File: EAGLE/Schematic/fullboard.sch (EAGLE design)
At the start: 101 parts, among them CN1 B4B-ZR, CN2 B4B-ZR, CN3 B4B-ZR, CN4 S4B-ZR, CN5 S4B-ZR, CN6 S4B-ZR, CN7 S4B-ZR, CN8 S4B-ZR, CN9 S4B-ZR, IC1 IFX007T, IC2 IFX007T, IC3 IFX007T, IC4 IFX007T, J1 10118193-0001LF, Q1 8MHz ±10ppm Crystal 18pF 80 O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, SW1 TR1-SPST, U1 ATXMEGA128A3U-AU, U2 FT232RL-REEL

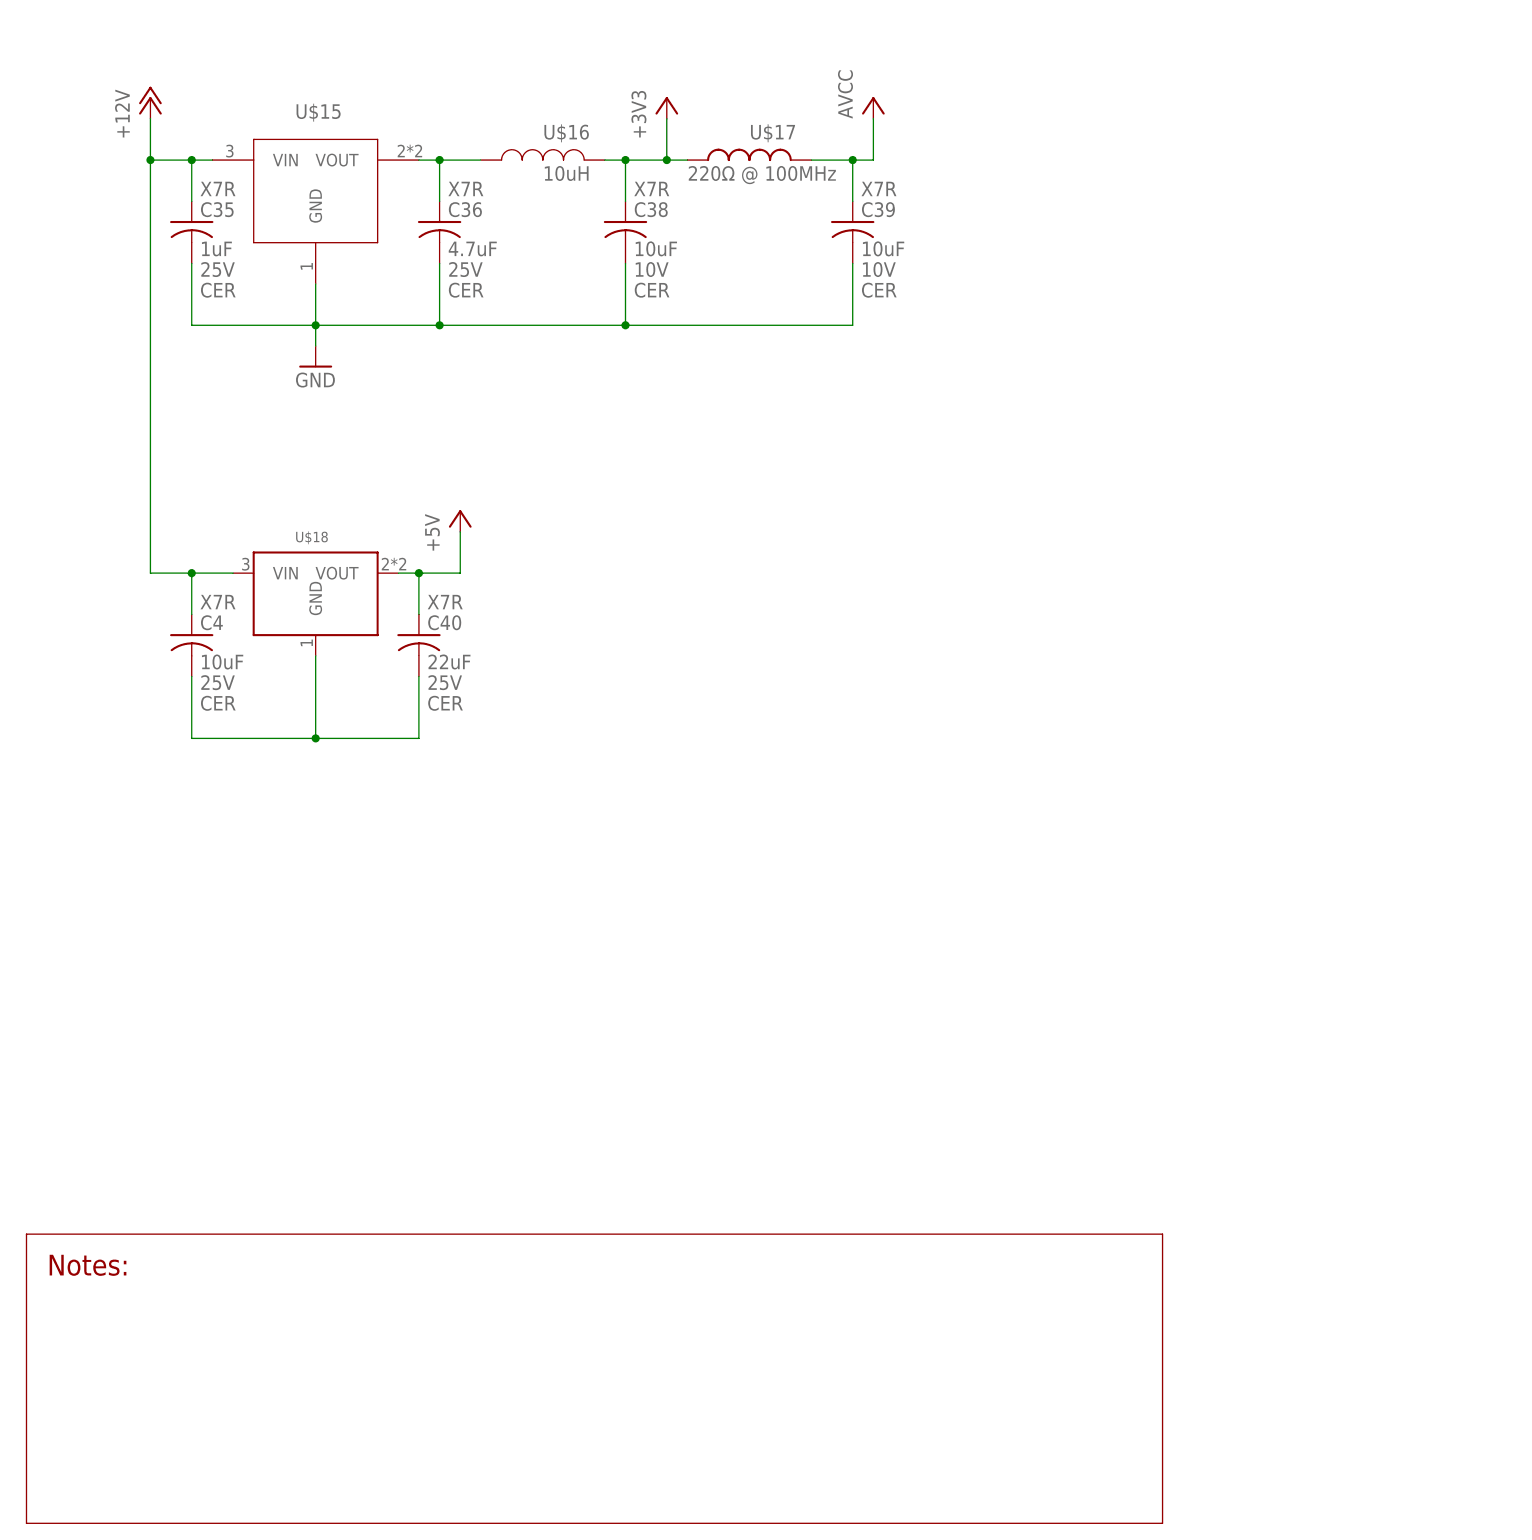
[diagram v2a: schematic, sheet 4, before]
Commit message: V0.3
Don't you dare put a fucking fuse holder on the board.

Added:
* Routing all the remaining signals
* Vias for breakout of leftover pins
* Now with 200% more suffering

Still to do:
* Things
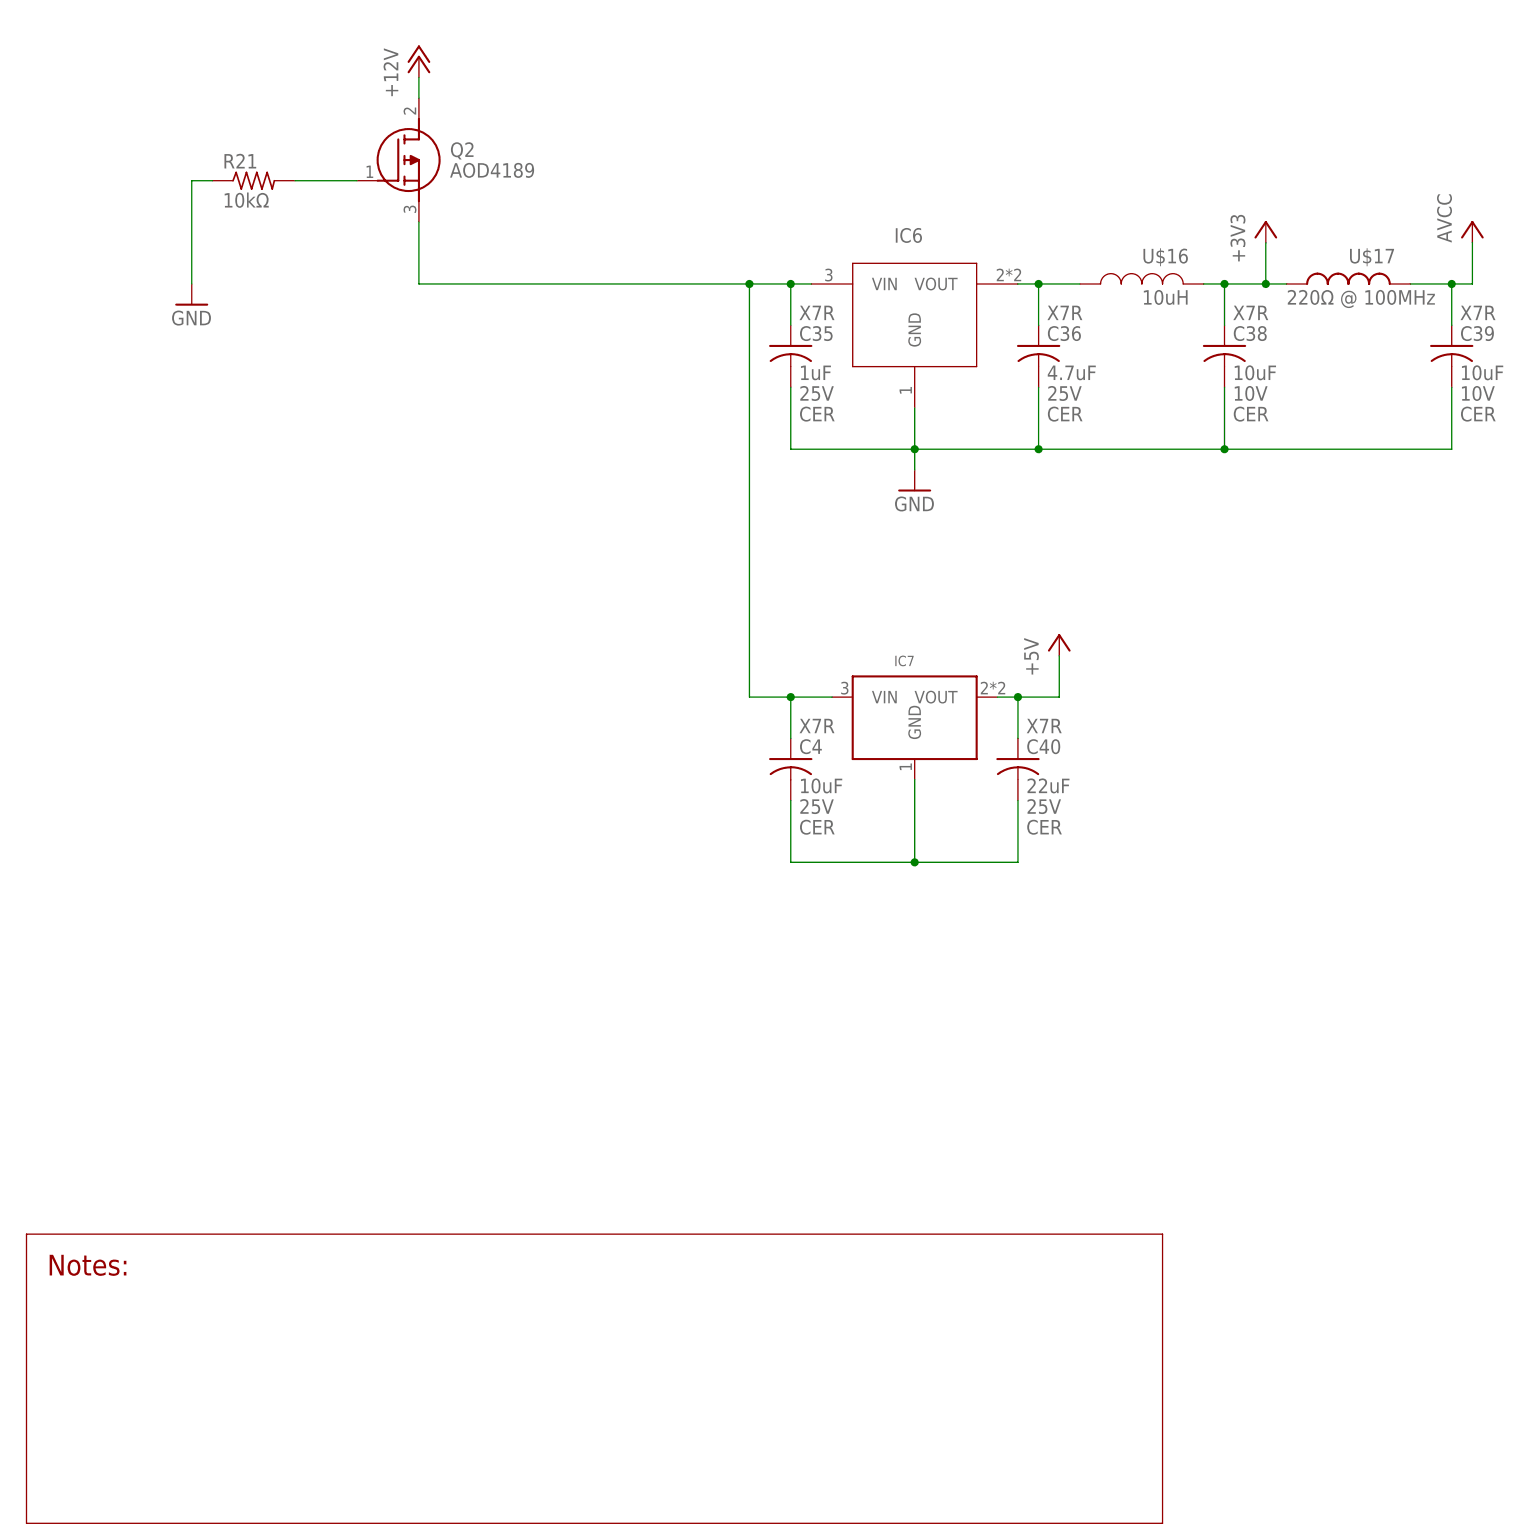
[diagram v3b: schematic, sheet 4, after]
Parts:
- added IC6: LDL1117S33R, SumBot:LDL1117S33R
- added IC7: AZ1117IH, SumBot:AZ1117IH
- added Q2: AOD4189, AOD4189:AOD4189
- added R20: 47Ω, rcl:R-US_R0805
- added R21: 10kΩ, rcl:R-US_R0805
- added U$19, U$20, U$21, U$22, U$23, U$24, U$25, U$26, U$27, U$28, U$29, U$30: NC, ME507:NC
- U$15: value LDL1117S33R -> NC; device SumBot:LDL1117S33R -> ME507:NC
- U$18: value AZ1117IH -> NC; device SumBot:AZ1117IH -> ME507:NC
- renumbered U2 to IC5
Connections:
- removed net CS_A: C11.1, C16.1, IC1.IS, IC2.IS, R3.2, R6.2
- removed net CS_B: C22.1, C27.1, IC3.IS, IC4.IS, R11.2, R14.2
- new net N$14: R20.1, U1A.PC7
- new net N$36: C35.1, C4.1, IC6.VIN, IC7.VIN, Q2.S
- new net N$37: Q2.G, R21.2
- new net N$38: U$23.D, U1A.PF0
- new net N$39: U$24.D, U1A.PF1
- new net N$40: U$25.D, U1A.PF2
- new net N$41: U$26.D, U1A.PF3
- new net N$42: U$27.D, U1A.PF4
- new net N$43: U$28.D, U1A.PF5
- new net N$44: U$22.D, U1A.PD7
- new net N$45: U$21.D, U1A.PD6
- new net N$46: U$20.D, U1A.PD5
- new net N$47: U$19.D, U1A.PD4
- new net N$48: U$18.D, U1A.PD3
- new net N$49: U$15.D, U1A.PD2
- new net N$50: U$29.D, U1A.PA0
- new net N$51: U$30.D, U1A.PA1
- net +12V: now also Q2.D; no longer C35.1, C4.1, U$15.VIN, U$18.VIN
- net +5V: now also IC7.VOUT; no longer U$18.VOUT
- net CSB_A: now also C16.1, IC2.IS, R6.2
- net CSB_B: now also C27.1, IC4.IS, R14.2
- net CSF_A: now also C11.1, IC1.IS, R3.2
- net CSF_B: now also C22.1, IC3.IS, R11.2
- net GND: now also IC6.GND, R21.1; no longer U$15.GND
- net N$1: now also IC7.GND; no longer U$18.GND
- net N$8: now also IC6.VOUT; no longer U$15.VOUT
- net TX/RX_MSE: now also R20.2; no longer U1A.PC7
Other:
- note added: "2. Check resistor wattage ratings again 3. Check feasibility of connecting both current sensing pins together"
- note removed: "2. Need testing to determine 3.3V function - spec is 5V. 3. Check resistor wattage ratings again 4. Check feasibility of connecting both current sensing pins together"
- moved on the sheet: C35, C36, C38, C39, C4, C40, U$16, U$17

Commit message: v0.5
Changes/Status
* Silkscreen - done, do a final check after walking away for a bit
* Mounting - #4 screws - moved the ones I could the way I could
* AREF - should be ok, made vias for use of jumpering if needed.

Todo:
* Final check by Charlie
* ...
* profit
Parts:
- added BATT: (no value), ME507:SCREWTERM_2P_508
- renumbered CN4 to E_A, CN5 to E_B, CN6 to E_C, CN7 to E_D, CN8 to E_E, CN9 to E_F, U$16 to L1, U$17 to L2
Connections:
- net +12V: now also BATT-2.1
- net GND: now also BATT-1.1

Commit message: V1.0
Final version board design
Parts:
- removed BATT: (no value), ME507:SCREWTERM_2P_508
- removed E_A, E_B, E_C, E_D, E_E, E_F: S4B-ZR, jst:S4B-ZR
- removed IC6: LDL1117S33R, SumBot:LDL1117S33R
- removed IC7: AZ1117IH, SumBot:AZ1117IH
- removed L1: RLB0914-100KL, SumBot:RLB0914-100KL
- removed L2: BLM21PG221SN1D, blm21:BLM21PG221SN1D
- removed Q2: AOD4189, AOD4189:AOD4189
- removed R20: 47Ω, rcl:R-US_R0805
- removed R21: 10kΩ, rcl:R-US_R0805
- removed U$19, U$20, U$21, U$22, U$23, U$24, U$25, U$26, U$27, U$28, U$29, U$30: NC, ME507:NC
- added U$16: RLB0914-100KL, SumBot:RLB0914-100KL
- added U$17: BLM21PG221SN1D, blm21:BLM21PG221SN1D
- CN1, CN2, CN3: value B4B-ZR -> B4B-XH-A; device jst:B4B-ZR -> jst:B4B-XH-A
- U$15: value NC -> LDL1117S33R; device ME507:NC -> SumBot:LDL1117S33R
- U$18: value NC -> AZ1117IH; device ME507:NC -> SumBot:AZ1117IH
- renumbered IC5 to U2
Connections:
- removed net EDGE_CTRL: E_A.4, E_B.4, E_C.4, E_D.4, E_E.4, E_F.4, U1A.PC0
- removed net N$14: R20.1, U1A.PC7
- removed net N$36: C35.1, C4.1, IC6.VIN, IC7.VIN, Q2.S
- removed net N$37: Q2.G, R21.2
- removed net N$38: U$23.D, U1A.PF0
- removed net N$39: U$24.D, U1A.PF1
- removed net N$40: U$25.D, U1A.PF2
- removed net N$41: U$26.D, U1A.PF3
- removed net N$42: U$27.D, U1A.PF4
- removed net N$43: U$28.D, U1A.PF5
- removed net N$44: U$22.D, U1A.PD7
- removed net N$45: U$21.D, U1A.PD6
- removed net N$46: U$20.D, U1A.PD5
- removed net N$47: U$19.D, U1A.PD4
- removed net N$48: U$18.D, U1A.PD3
- removed net N$49: U$15.D, U1A.PD2
- removed net N$50: U$29.D, U1A.PA0
- removed net N$51: U$30.D, U1A.PA1
- new net CS_A: C11.1, C16.1, IC1.IS, IC2.IS, R3.2, R6.2
- new net CS_B: C22.1, C27.1, IC3.IS, IC4.IS, R11.2, R14.2
- net +12V: now also C35.1, C4.1, U$15.VIN, U$18.VIN; no longer BATT-2.1, Q2.D
- net +3V3: now also U$16.P$2, U$17.1; no longer E_A.2, E_B.2, E_C.2, E_D.2, E_E.2, E_F.2, L1.P$2, L2.1
- net +5V: now also U$18.VOUT; no longer IC7.VOUT
- net AVCC: now also U$17.2; no longer L2.2
- net BCK_A: now also U1A.PD1; no longer U1A.PE5
- net BCK_B: now also U1A.PD3; no longer U1A.PE2
- net CSB_A: no longer C16.1, IC2.IS, R6.2
- net CSB_B: no longer C27.1, IC4.IS, R14.2
- net CSF_A: no longer C11.1, IC1.IS, R3.2
- net CSF_B: no longer C22.1, IC3.IS, R11.2
- net EA_A: now also U1A.PF4; no longer U1A.PF6
- net EA_B: now also U1A.PF1; no longer U1A.PD1
- net EB_A: now also U1A.PF5; no longer U1A.PF7
- net EB_B: now also U1A.PF2; no longer U1A.PD0
- net EDGE_A: now also U1A.PA0; no longer E_A.1, U1A.PA2
- net EDGE_B: now also U1A.PA1; no longer E_B.1, U1A.PA3
- net EDGE_C: now also U1A.PA2; no longer E_C.1, U1A.PA4
- net EDGE_D: now also U1A.PA3; no longer E_D.1, U1A.PA5
- net EDGE_E: now also U1A.PA4; no longer E_E.1, U1A.PA6
- net EDGE_F: now also U1A.PA5; no longer E_F.1, U1A.PA7
- net EN_A: now also U1A.PF3; no longer U1A.PE6
- net EN_B: now also U1A.PF0; no longer U1A.PE1
- net FWD_A: now also U1A.PD0; no longer U1A.PE4
- net FWD_B: now also U1A.PD2; no longer U1A.PE3
- net GND: now also U$15.GND; no longer BATT-1.1, E_A.3, E_B.3, E_C.3, E_D.3, E_E.3, E_F.3, IC6.GND, R21.1
- net N$1: now also U$18.GND; no longer IC7.GND
- net N$8: now also U$15.VOUT, U$16.P$3; no longer IC6.VOUT, L1.P$3
- net TX/RX_MSE: now also U1A.PC5; no longer R20.2
- net XCK_MSE: now also U1A.PC4; no longer U1A.PC5
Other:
- note added: "2. Need testing to determine 3.3V function - spec is 5V. 3. Check resistor wattage ratings again 4. Check feasibility of connecting both current sensing pins together"
- note removed: "2. Check resistor wattage ratings again 3. Check feasibility of connecting both current sensing pins together"
- note removed: "EDGE_(A-F) represent the sensor output voltage which ranges from 0 V to Vcc provided to sensor EDGE_CTRL is the LED emitter current control pin"
